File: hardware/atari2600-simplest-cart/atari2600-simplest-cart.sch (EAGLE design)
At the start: 4 parts, among them CON1 24PINEDGE-ATARI-2600, IC3 74S04N

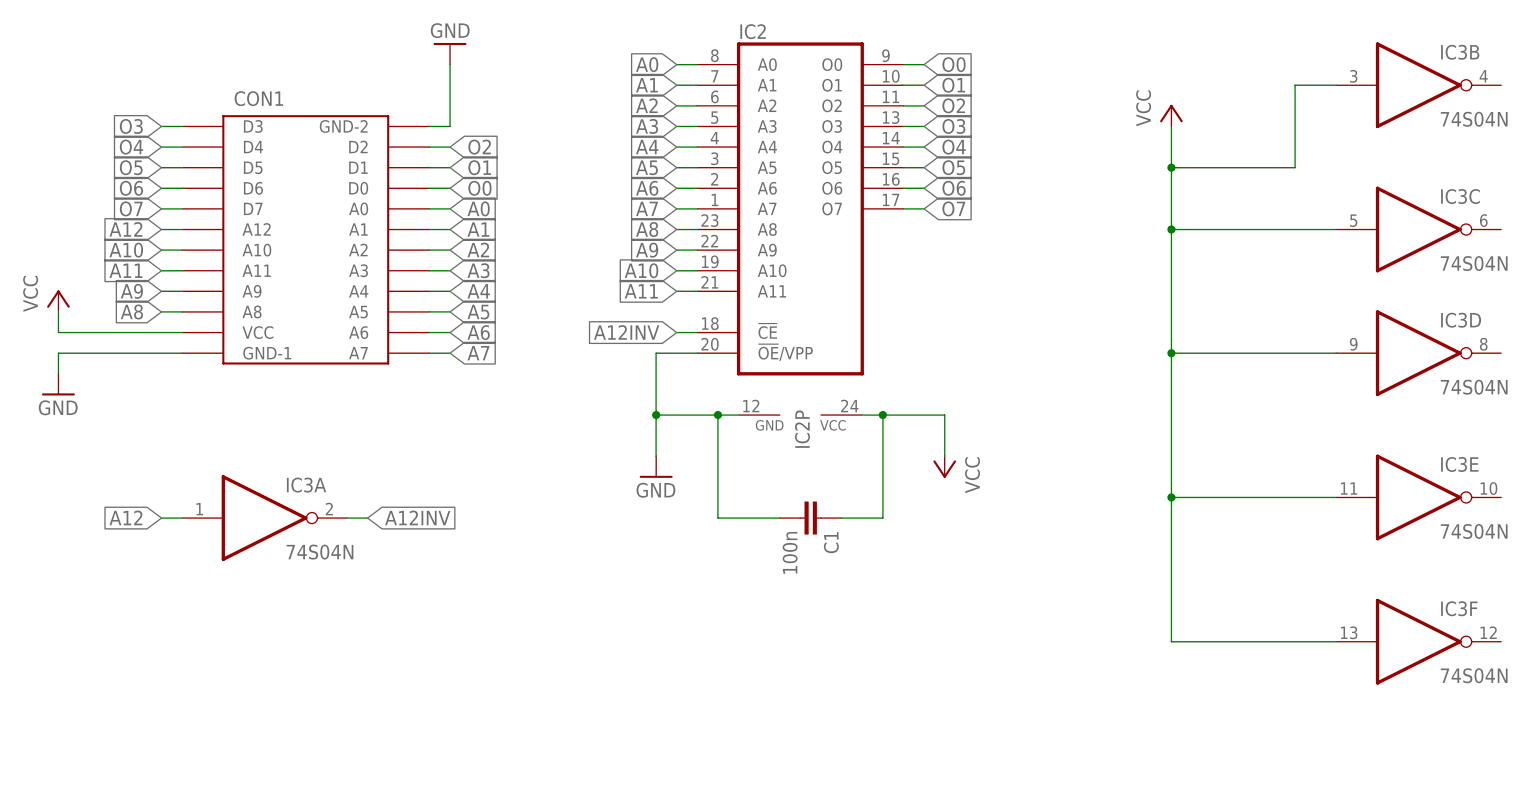
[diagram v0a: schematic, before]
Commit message: Replace IC inverter with transistor based inverter on PCB
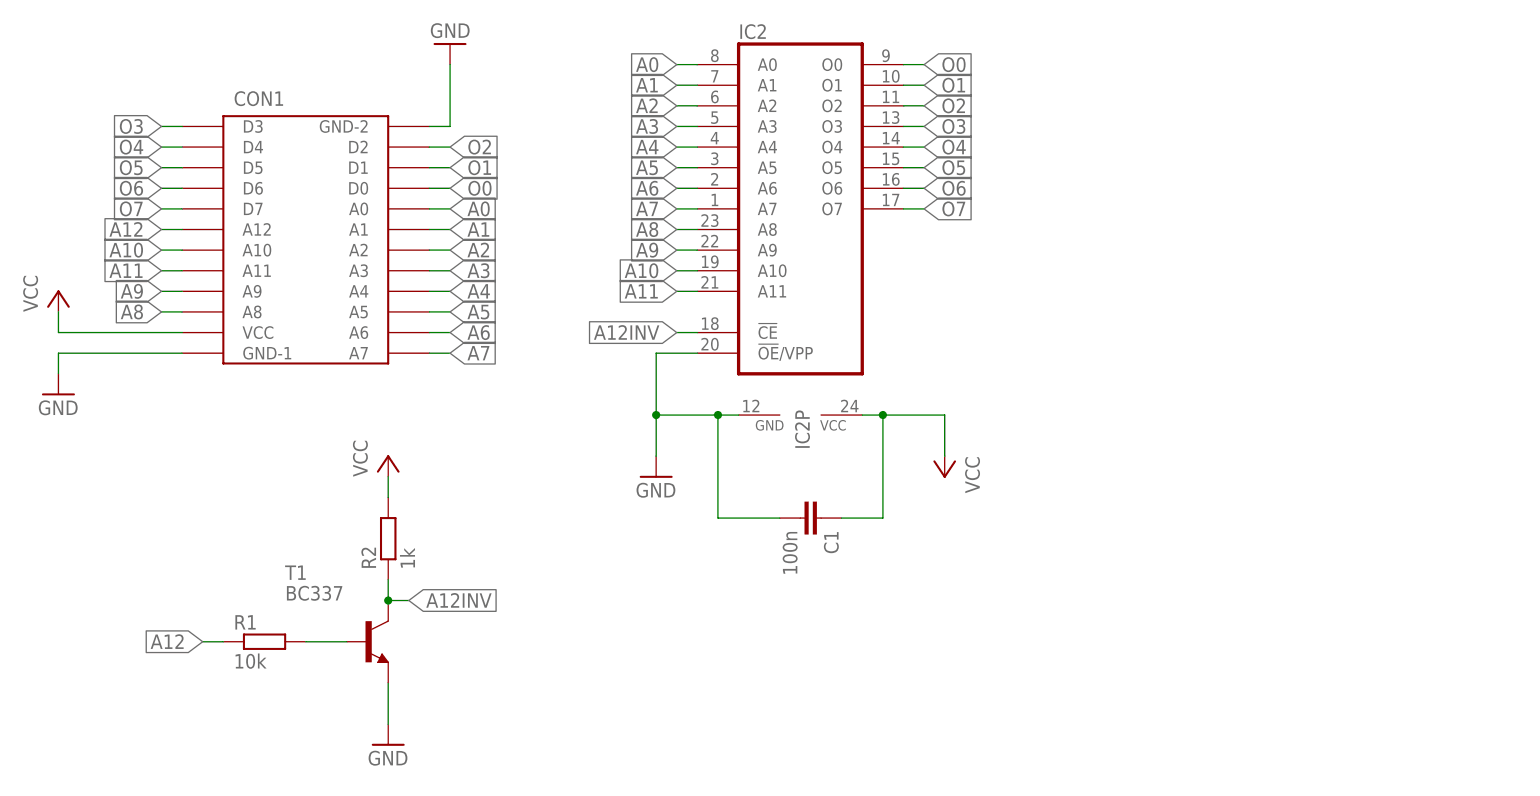
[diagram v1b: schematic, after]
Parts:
- removed IC3: 74S04N, 74xx-eu:74S04N
- added R1: 10k, rcl:R-EU_0204/7
- added R2: 1k, rcl:R-EU_0204/7
- added T1: BC337, transistor:BC337
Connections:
- new net N$2: R1.2, T1.B
- net A12: now also R1.1; no longer IC3A.I
- net A12INV: now also R2.1, T1.C; no longer IC3A.O
- net GND: now also T1.E
- net VCC: now also R2.2; no longer IC3B.I, IC3C.I, IC3D.I, IC3E.I, IC3F.I
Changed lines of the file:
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@@
 <part name="GND1" library="supply1" library_urn="urn:adsk.eagle:library:371" deviceset="GND" device=""/>
 <part name="P+2" library="supply1" library_urn="urn:adsk.eagle:library:371" deviceset="VCC" device=""/>
-<part name="IC3" library="74xx-eu" library_urn="urn:adsk.eagle:library:85" deviceset="74*04" device="N" package3d_urn="urn:adsk.eagle:package:16407/2" technology="S"/>
-<part name="P+4" library="supply1" library_urn="urn:adsk.eagle:library:371" deviceset="VCC" device=""/>
 <part name="GND5" library="supply1" library_urn="urn:adsk.eagle:library:371" deviceset="GND" device=""/>
 <part name="IC2" library="memory" library_urn="urn:adsk.eagle:library:279" deviceset="2732" device="" package3d_urn="urn:adsk.eagle:package:19955/2"/>
 <part name="GND2" library="supply1" library_urn="urn:adsk.eagle:library:371" deviceset="GND" device=""/>
 <part name="C1" library="rcl" library_urn="urn:adsk.eagle:library:334" deviceset="C-EU" device="025-025X050" package3d_urn="urn:adsk.eagle:package:23629/2" value="100n"/>
+<part name="T1" library="transistor" library_urn="urn:adsk.eagle:library:402" deviceset="BC337" device="" package3d_urn="urn:adsk.eagle:package:28523/2"/>
+<part name="R1" library="rcl" library_urn="urn:adsk.eagle:library:334" deviceset="R-EU_" device="0204/7" package3d_urn="urn:adsk.eagle:package:23498/2" value="10k"/>
+<part name="R2" library="rcl" library_urn="urn:adsk.eagle:library:334" deviceset="R-EU_" device="0204/7" package3d_urn="urn:adsk.eagle:package:23498/2" value="1k"/>
+<part name="GND3" library="supply1" library_urn="urn:adsk.eagle:library:371" deviceset="GND" device=""/>
+<part name="P+3" library="supply1" library_urn="urn:adsk.eagle:library:371" deviceset="VCC" device=""/>
 </parts>
 <sheets>
@@
 <attribute name="VALUE" x="127" y="40.64" size="1.778" layer="96" rot="R270"/>
 </instance>
-<instance part="IC3" gate="A" x="40.64" y="33.02" smashed="yes">
-<attribute name="NAME" x="43.18" y="36.195" size="1.778" layer="95"/>
-<attribute name="VALUE" x="43.18" y="27.94" size="1.778" layer="96"/>
-</instance>
-<instance part="IC3" gate="B" x="182.88" y="86.36" smashed="yes">
-<attribute name="NAME" x="185.42" y="89.535" size="1.778" layer="95"/>
-<attribute name="VALUE" x="185.42" y="81.28" size="1.778" layer="96"/>
-</instance>
-<instance part="IC3" gate="C" x="182.88" y="68.58" smashed="yes">
-<attribute name="NAME" x="185.42" y="71.755" size="1.778" layer="95"/>
-<attribute name="VALUE" x="185.42" y="63.5" size="1.778" layer="96"/>
-</instance>
-<instance part="IC3" gate="D" x="182.88" y="53.34" smashed="yes">
-<attribute name="NAME" x="185.42" y="56.515" size="1.778" layer="95"/>
-<attribute name="VALUE" x="185.42" y="48.26" size="1.778" layer="96"/>
-</instance>
-<instance part="IC3" gate="E" x="182.88" y="35.56" smashed="yes">
-<attribute name="NAME" x="185.42" y="38.735" size="1.778" layer="95"/>
-<attribute name="VALUE" x="185.42" y="30.48" size="1.778" layer="96"/>
-</instance>
-<instance part="IC3" gate="F" x="182.88" y="17.78" smashed="yes">
-<attribute name="NAME" x="185.42" y="20.955" size="1.778" layer="95"/>
-<attribute name="VALUE" x="185.42" y="12.7" size="1.778" layer="96"/>
-</instance>
-<instance part="P+4" gate="VCC" x="152.4" y="83.82" smashed="yes">
-<attribute name="VALUE" x="149.86" y="81.28" size="1.778" layer="96" rot="R90"/>
-</instance>
 <instance part="GND5" gate="1" x="63.5" y="91.44" smashed="yes" rot="R180">
 <attribute name="VALUE" x="66.04" y="93.98" size="1.778" layer="96" rot="R180"/>
@@
 <attribute name="NAME" x="109.601" y="31.496" size="1.778" layer="95" rot="R270"/>
 <attribute name="VALUE" x="104.521" y="31.496" size="1.778" layer="96" rot="R270"/>
+</instance>
+<instance part="T1" gate="G$1" x="53.34" y="17.78" smashed="yes">
+<attribute name="NAME" x="43.18" y="25.4" size="1.778" layer="95"/>
+<attribute name="VALUE" x="43.18" y="22.86" size="1.778" layer="96"/>
+</instance>
+<instance part="R1" gate="G$1" x="40.64" y="17.78" smashed="yes">
+<attribute name="NAME" x="36.83" y="19.2786" size="1.778" layer="95"/>
+<attribute name="VALUE" x="36.83" y="14.478" size="1.778" layer="96"/>
+</instance>
+<instance part="R2" gate="G$1" x="55.88" y="30.48" smashed="yes" rot="R90">
+<attribute name="NAME" x="54.3814" y="26.67" size="1.778" layer="95" rot="R90"/>
+<attribute name="VALUE" x="59.182" y="26.67" size="1.778" layer="96" rot="R90"/>
+</instance>
+<instance part="GND3" gate="1" x="55.88" y="5.08" smashed="yes">
+<attribute name="VALUE" x="53.34" y="2.54" size="1.778" layer="96"/>
+</instance>
+<instance part="P+3" gate="VCC" x="55.88" y="40.64" smashed="yes">
+<attribute name="VALUE" x="53.34" y="38.1" size="1.778" layer="96" rot="R90"/>
 </instance>
 </instances>
@@
 <pinref part="CON1" gate="G$1" pin="VCC"/>
 <wire x1="15.24" y1="55.88" x2="30.48" y2="55.88" width="0.1524" layer="91"/>
-</segment>
-<segment>
-<pinref part="P+4" gate="VCC" pin="VCC"/>
-<wire x1="152.4" y1="81.28" x2="152.4" y2="76.2" width="0.1524" layer="91"/>
-<pinref part="IC3" gate="F" pin="I"/>
-<wire x1="152.4" y1="76.2" x2="152.4" y2="68.58" width="0.1524" layer="91"/>
-<wire x1="152.4" y1="68.58" x2="152.4" y2="53.34" width="0.1524" layer="91"/>
-<wire x1="152.4" y1="53.34" x2="152.4" y2="35.56" width="0.1524" layer="91"/>
-<wire x1="152.4" y1="35.56" x2="152.4" y2="17.78" width="0.1524" layer="91"/>
-<wire x1="152.4" y1="17.78" x2="172.72" y2="17.78" width="0.1524" layer="91"/>
-<pinref part="IC3" gate="E" pin="I"/>
-<wire x1="152.4" y1="35.56" x2="172.72" y2="35.56" width="0.1524" layer="91"/>
-<junction x="152.4" y="35.56"/>
-<pinref part="IC3" gate="D" pin="I"/>
-<wire x1="152.4" y1="53.34" x2="172.72" y2="53.34" width="0.1524" layer="91"/>
-<junction x="152.4" y="53.34"/>
-<pinref part="IC3" gate="C" pin="I"/>
-<wire x1="152.4" y1="68.58" x2="172.72" y2="68.58" width="0.1524" layer="91"/>
-<junction x="152.4" y="68.58"/>
-<wire x1="152.4" y1="76.2" x2="167.64" y2="76.2" width="0.1524" layer="91"/>
-<junction x="152.4" y="76.2"/>
-<wire x1="167.64" y1="76.2" x2="167.64" y2="86.36" width="0.1524" layer="91"/>
-<pinref part="IC3" gate="B" pin="I"/>
-<wire x1="167.64" y1="86.36" x2="172.72" y2="86.36" width="0.1524" layer="91"/>
 </segment>
 <segment>
@@
 <wire x1="116.84" y1="33.02" x2="116.84" y2="45.72" width="0.1524" layer="91"/>
 <junction x="116.84" y="45.72"/>
+</segment>
+<segment>
+<pinref part="P+3" gate="VCC" pin="VCC"/>
+<pinref part="R2" gate="G$1" pin="2"/>
+<wire x1="55.88" y1="38.1" x2="55.88" y2="35.56" width="0.1524" layer="91"/>
 </segment>
 </net>
@@
 <junction x="96.52" y="45.72"/>
 </segment>
+<segment>
+<pinref part="GND3" gate="1" pin="GND"/>
+<pinref part="T1" gate="G$1" pin="E"/>
+<wire x1="55.88" y1="7.62" x2="55.88" y2="12.7" width="0.1524" layer="91"/>
+</segment>
 </net>
 <net name="A0" class="0">
@@
 </segment>
 <segment>
-<pinref part="IC3" gate="A" pin="I"/>
-<wire x1="30.48" y1="33.02" x2="27.94" y2="33.02" width="0.1524" layer="91"/>
-<label x="27.94" y="33.02" size="1.778" layer="95" rot="R180" xref="yes"/>
+<pinref part="R1" gate="G$1" pin="1"/>
+<wire x1="35.56" y1="17.78" x2="33.02" y2="17.78" width="0.1524" layer="91"/>
+<label x="33.02" y="17.78" size="1.778" layer="95" rot="R180" xref="yes"/>
 </segment>
 </net>
 <net name="A12INV" class="0">
-<segment>
-<pinref part="IC3" gate="A" pin="O"/>
-<wire x1="50.8" y1="33.02" x2="53.34" y2="33.02" width="0.1524" layer="91"/>
-<label x="53.34" y="33.02" size="1.778" layer="95" xref="yes"/>
-</segment>
 <segment>
 <pinref part="IC2" gate="A" pin="!CE"/>
@@
 <label x="91.44" y="55.88" size="1.778" layer="95" rot="R180" xref="yes"/>
 </segment>
-</net>
+<segment>
+<pinref part="R2" gate="G$1" pin="1"/>
+<pinref part="T1" gate="G$1" pin="C"/>
+<wire x1="55.88" y1="25.4" x2="55.88" y2="22.86" width="0.1524" layer="91"/>
+<wire x1="55.88" y1="22.86" x2="58.42" y2="22.86" width="0.1524" layer="91"/>
+<junction x="55.88" y="22.86"/>
+<label x="58.42" y="22.86" size="1.778" layer="95" xref="yes"/>
+</segment>
+</net>
+<net name="N$2" class="0">
+<segment>
+<pinref part="R1" gate="G$1" pin="2"/>
+<pinref part="T1" gate="G$1" pin="B"/>
+<wire x1="45.72" y1="17.78" x2="50.8" y2="17.78" width="0.1524" layer="91"/>
+</segment>
+</net>

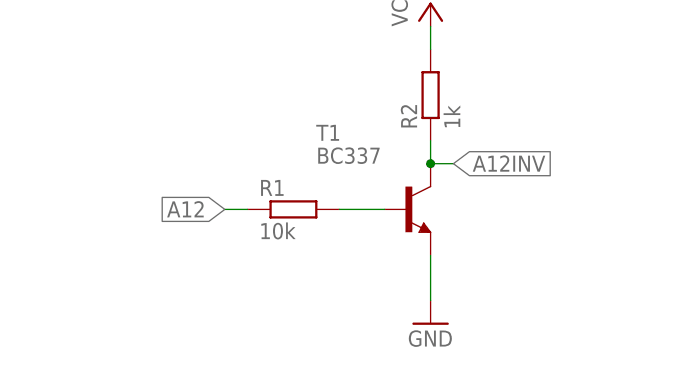
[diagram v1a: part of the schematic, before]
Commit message: Add missing capacitor to the cartridge board schematic
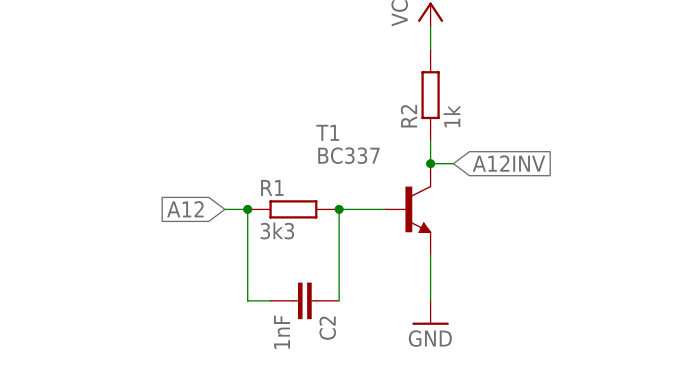
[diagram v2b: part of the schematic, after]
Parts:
- added C2: 1nF, rcl:C-EU025-025X050
- R1: value 10k -> 3k3
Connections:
- net A12: now also C2.2
- net N$2: now also C2.1
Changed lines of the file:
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@@
 <part name="C1" library="rcl" library_urn="urn:adsk.eagle:library:334" deviceset="C-EU" device="025-025X050" package3d_urn="urn:adsk.eagle:package:23629/2" value="100n"/>
 <part name="T1" library="transistor" library_urn="urn:adsk.eagle:library:402" deviceset="BC337" device="" package3d_urn="urn:adsk.eagle:package:28523/2"/>
-<part name="R1" library="rcl" library_urn="urn:adsk.eagle:library:334" deviceset="R-EU_" device="0204/7" package3d_urn="urn:adsk.eagle:package:23498/2" value="10k"/>
+<part name="R1" library="rcl" library_urn="urn:adsk.eagle:library:334" deviceset="R-EU_" device="0204/7" package3d_urn="urn:adsk.eagle:package:23498/2" value="3k3"/>
 <part name="R2" library="rcl" library_urn="urn:adsk.eagle:library:334" deviceset="R-EU_" device="0204/7" package3d_urn="urn:adsk.eagle:package:23498/2" value="1k"/>
 <part name="GND3" library="supply1" library_urn="urn:adsk.eagle:library:371" deviceset="GND" device=""/>
 <part name="P+3" library="supply1" library_urn="urn:adsk.eagle:library:371" deviceset="VCC" device=""/>
+<part name="C2" library="rcl" library_urn="urn:adsk.eagle:library:334" deviceset="C-EU" device="025-025X050" package3d_urn="urn:adsk.eagle:package:23629/2" value="1nF"/>
 </parts>
 <sheets>
@@
 <instance part="P+3" gate="VCC" x="55.88" y="40.64" smashed="yes">
 <attribute name="VALUE" x="53.34" y="38.1" size="1.778" layer="96" rot="R90"/>
+</instance>
+<instance part="C2" gate="G$1" x="43.18" y="7.62" smashed="yes" rot="R270">
+<attribute name="NAME" x="43.561" y="6.096" size="1.778" layer="95" rot="R270"/>
+<attribute name="VALUE" x="38.481" y="6.096" size="1.778" layer="96" rot="R270"/>
 </instance>
 </instances>
@@
 <wire x1="35.56" y1="17.78" x2="33.02" y2="17.78" width="0.1524" layer="91"/>
 <label x="33.02" y="17.78" size="1.778" layer="95" rot="R180" xref="yes"/>
+<wire x1="35.56" y1="17.78" x2="35.56" y2="7.62" width="0.1524" layer="91"/>
+<junction x="35.56" y="17.78"/>
+<pinref part="C2" gate="G$1" pin="2"/>
+<wire x1="35.56" y1="7.62" x2="38.1" y2="7.62" width="0.1524" layer="91"/>
 </segment>
 </net>
@@
 <pinref part="T1" gate="G$1" pin="B"/>
 <wire x1="45.72" y1="17.78" x2="50.8" y2="17.78" width="0.1524" layer="91"/>
-</segment>
-</net>
+<pinref part="C2" gate="G$1" pin="1"/>
+<wire x1="45.72" y1="7.62" x2="45.72" y2="17.78" width="0.1524" layer="91"/>
+<junction x="45.72" y="17.78"/>
+</segment>
+</net>
